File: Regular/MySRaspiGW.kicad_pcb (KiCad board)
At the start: 2 copper layers, 11.5 x 11.9 mm, 5 parts, among them P1 CONN_02X04, U1 NRF24L01

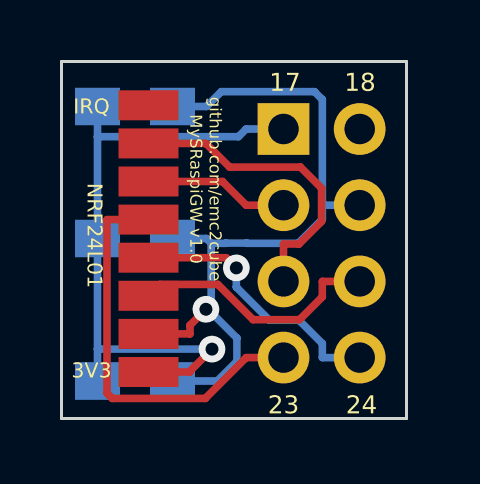
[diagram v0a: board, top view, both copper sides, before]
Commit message: v1.1 IRQ support
Added IRQ support on pin 18
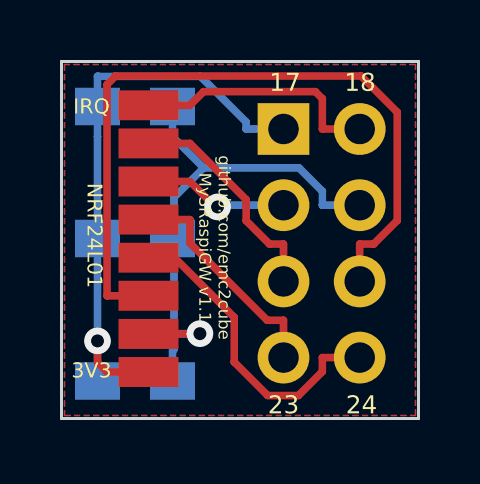
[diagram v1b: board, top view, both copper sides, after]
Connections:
- P1 pad 2: Net-(P1-Pad2) -> IRQ
- U1 pad 8: Net-(U1-Pad8) -> IRQ
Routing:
- net CE: track 8.51 -> 25.1 mm
- net IRQ: track 0.00 -> 8.34 mm
- net GND: track 25.3 -> 18.6 mm
- net SCK: track 13.7 -> 7.59 mm
- net MISO: track 10.3 -> 7.55 mm
- net +3V3: track 21.7 -> 19.8 mm
- net CSN: track 9.07 -> 10.6 mm, vias 1 -> 0
- net MOSI: track 4.83 -> 4.87 mm, vias 0 -> 1
- added copper zone on B.Cu, net GND
- added copper zone on F.Cu, net GND
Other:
- board size 11.5 x 11.9 mm -> 11.9 x 11.9 mm
- board text added: "github.com/emc2cube MySRaspiGW v1.1"
- board text removed: "github.com/emc2cube MySRaspiGW v1.0"
